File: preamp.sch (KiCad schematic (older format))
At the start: 12 parts

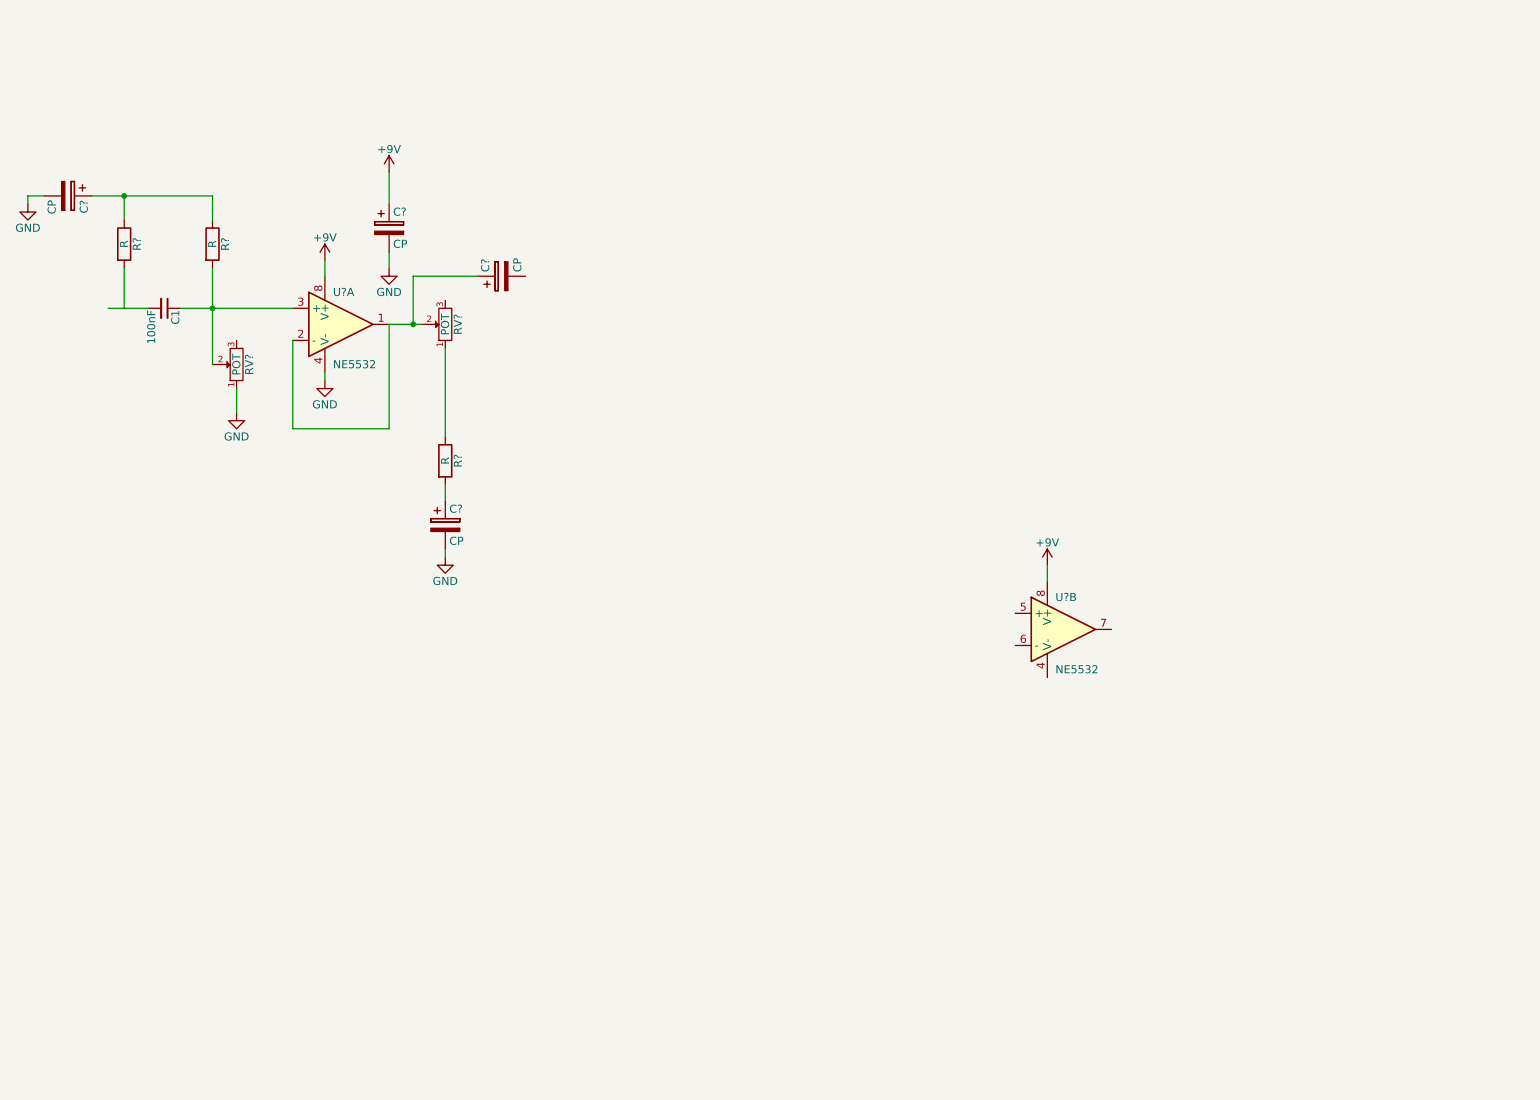
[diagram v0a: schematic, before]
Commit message: Esquemático e netlist gerados
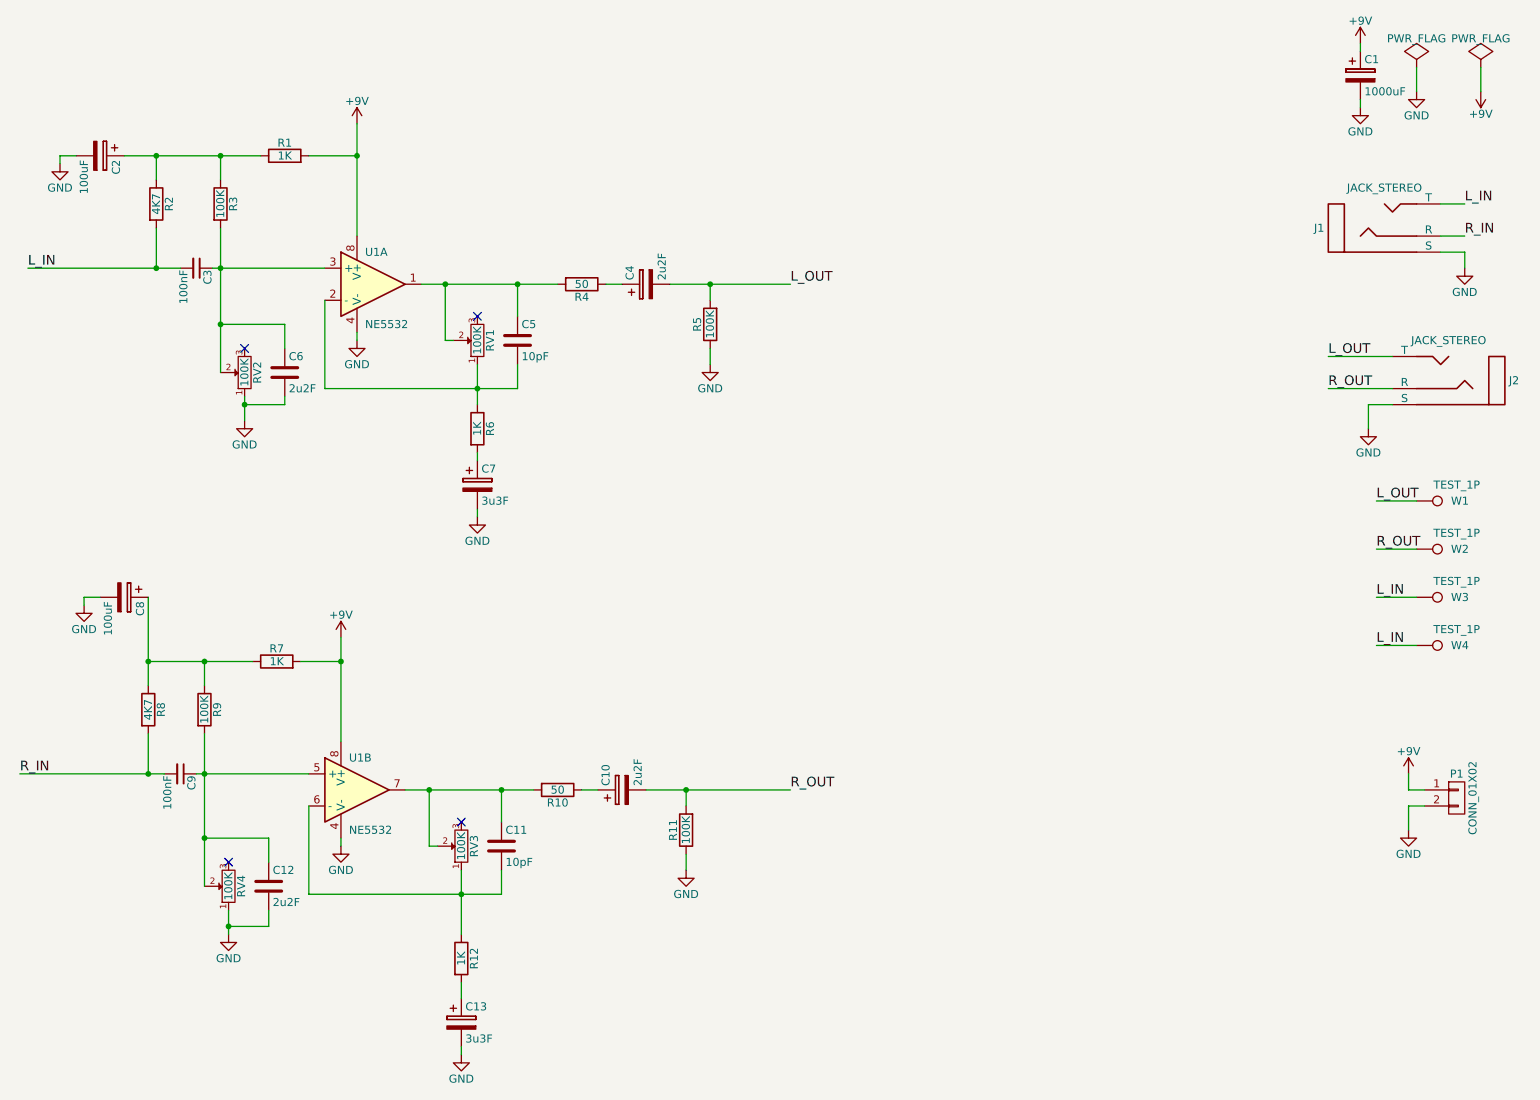
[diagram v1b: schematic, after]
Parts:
- removed C?: CP, symbol CP
- added C10, C4: 2u2F, symbol CP
- added C11, C5: 10pF, symbol C
- added C12, C6: 2u2F, symbol C
- added C13: 3u3F, symbol CP
- added C8: 100uF, symbol CP
- added C9: 100nF, symbol C_Small
- added J1, J2: JACK_STEREO, symbol JACK_STEREO
- added P1: CONN_01X02, symbol CONN_01X02
- added R1, R12, R7: 1K, symbol R
- added R10, R4: 50, symbol R
- added R11, R5, R9: 100K, symbol R
- added R8: 4K7, symbol R
- added RV3, RV4: 100K, symbol POT
- added W1, W2, W3, W4: TEST_1P, symbol TEST_1P
- C1: renamed from C?; value CP -> 1000uF
- C2: renamed from C?; value CP -> 100uF
- C7: renamed from C?; value CP -> 3u3F
- R2: renamed from R?; value R -> 4K7
- R3: renamed from R?; value R -> 100K
- R6: renamed from R?; value R -> 1K
- RV1, RV2: renamed from RV?; value POT -> 100K
- gave numbers to parts that had none: 1
- renumbered C1 to C3
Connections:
- net labels added: L_IN, L_OUT, R_IN, R_OUT
- wire segments 24 -> 82
- no-connect marks 0 -> 4
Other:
- moved on the sheet: C1, C2, C3, C7, R2, R3, R6, RV1, RV2, U1A, U1B

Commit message: pcb
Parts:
- removed C12, C6: 2u2F, symbol C
- removed J1, J2: JACK_STEREO, symbol JACK_STEREO
- added C12, C6: 2u2F, Capacitors_ThroughHole:C_Radial_D5_L11_P2.5, symbol CP
- added J1, J2: JACK_TRS_6PINS, Connect:PINHEAD1-6, symbol JACK_TRS_6PINS
- added P2: RCA_L, w_conn_av:rca_white, symbol CONNECTOR_2
- added P3: RCA_R, w_conn_av:rca_red, symbol CONNECTOR_2
- C1: footprint (none) -> Capacitors_ThroughHole:C_Radial_D10_L20_P5
- C10, C13, C4, C7: footprint (none) -> Capacitors_ThroughHole:C_Radial_D5_L11_P2.5
- C11, C5: footprint (none) -> Capacitors_ThroughHole:C_Disc_D6_P5
- C2, C8: footprint (none) -> Capacitors_ThroughHole:C_Radial_D6.3_L11.2_P2.5
- C3, C9: footprint (none) -> Capacitors_ThroughHole:C_Disc_D12_P7.75
- P1: footprint (none) -> Pin_Headers:Pin_Header_Straight_1x02
- R1, R10, R11, R12, R2, R3, R4, R5, R6, R7, R8, R9: footprint (none) -> Resistors_ThroughHole:Resistor_Horizontal_RM10mm
- RV1, RV2, RV3, RV4: footprint (none) -> Potentiometers:Potentiometer_WirePads
- U1: footprint (none) -> Housings_DIP:DIP-8_W7.62mm
- W1, W2, W3, W4: footprint (none) -> Measurement_Points:Measurement_Point_Round-SMD-Pad_Big
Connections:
- net GND: now also C12.2, C6.2, J1.1 (S), J2.1 (S), P2.2, P3.2
- net L_IN: now also J1.2 (T)
- net L_OUT: now also J2.2 (T), P2.1
- net R_IN: now also J1.3 (R)
- net R_OUT: now also J2.3 (R), P3.1
- net at C3.1, R3.2, RV2.2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: now also C6.1
- net at C9.1, R9.2, RV4.2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: now also C12.1
- no-connect marks 4 -> 10
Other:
- moved on the sheet: P1, W1, W2, W3, W4

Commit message: pcb roteada
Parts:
- removed J1, J2: JACK_TRS_6PINS, Connect:PINHEAD1-6, symbol JACK_TRS_6PINS
- added J1, J2: JACK_STEREO, audio_conn:audio_jack, symbol JACK_STEREO
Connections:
- net GND: now also RV2.3, J1.S, J2.S; no longer RV2.1
- net L_IN: now also J1.T; no longer W4.1
- net L_OUT: now also J2.T
- net R_IN: now also W4.1, J1.R
- net R_OUT: now also J2.R
- net at C11.2, R12.1, U1.6 (-): now also RV3.3; no longer RV3.1
- no-connect marks 10 -> 4
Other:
- moved on the sheet: C6, RV2, RV3

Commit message: nem sei
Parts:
- RV1, RV2, RV3, RV4: symbol POT -> POT-RESCUE-preamp
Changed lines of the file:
@@
 EESchema Schematic File Version 2
+LIBS:preamp-rescue
 LIBS:power
 LIBS:device
@@
 $EndComp
 $Comp
-L POT RV2
+L POT-RESCUE-preamp RV2
 U 1 1 57F1EC9D
 P 2650 2950
@@
 $EndComp
 $Comp
-L POT RV1
+L POT-RESCUE-preamp RV1
 U 1 1 57F1EDE3
 P 4250 2700
@@
 $EndComp
 $Comp
-L POT RV4
+L POT-RESCUE-preamp RV4
 U 1 1 57F46D6F
 P 2700 6100
@@
 $EndComp
 $Comp
-L POT RV3
+L POT-RESCUE-preamp RV3
 U 1 1 57F46D7B
 P 3950 5900
